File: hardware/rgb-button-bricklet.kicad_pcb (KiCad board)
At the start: 2 copper layers, 25 x 30 mm, 17 parts, among them P1 CON-SENSOR, P2 Boot, SW1 RGB_SWITCH_AD, U1 XMC1XXX24, U2 DRILL, U3 DRILL, U4 DRILL, U5 DRILL

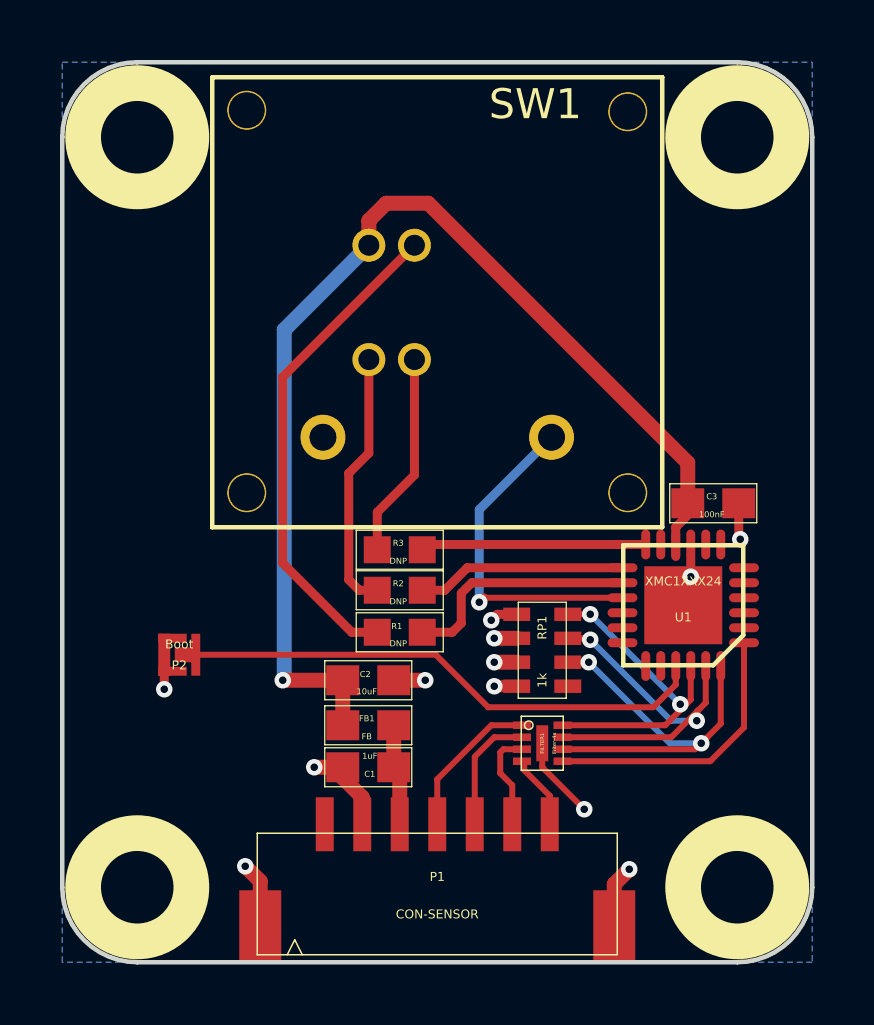
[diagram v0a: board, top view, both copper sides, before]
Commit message: Add fiducial marks and TF logo
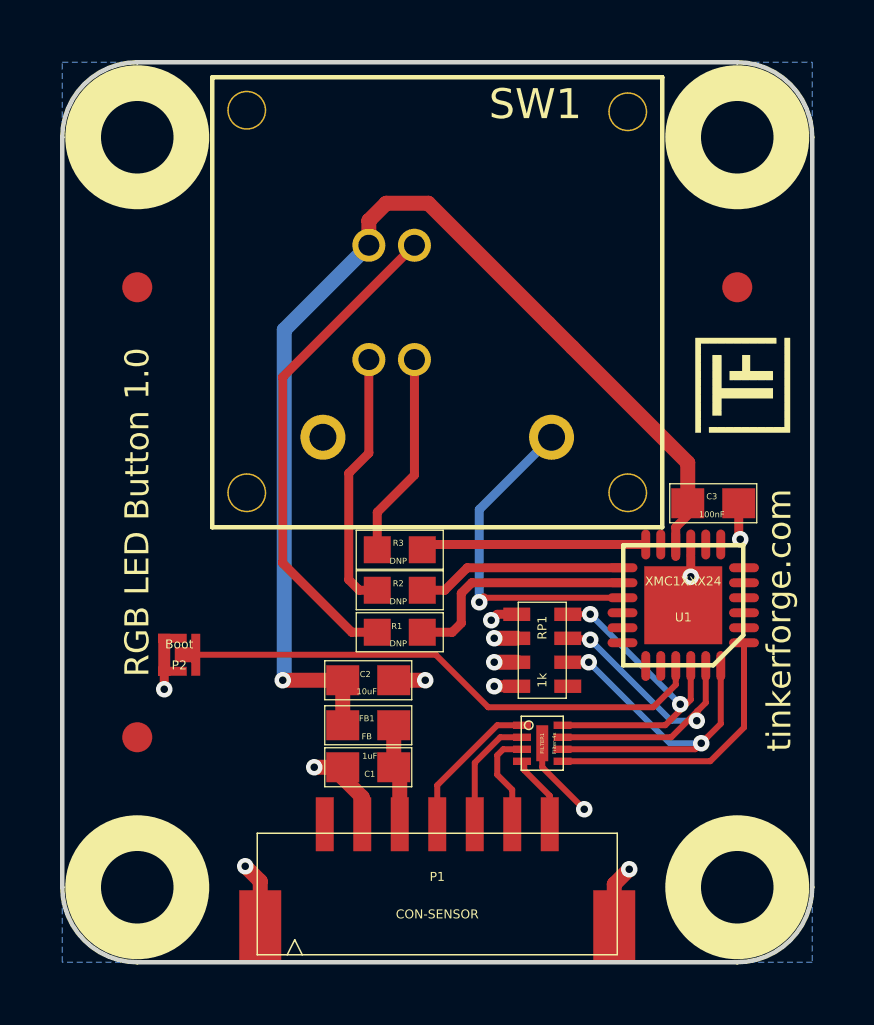
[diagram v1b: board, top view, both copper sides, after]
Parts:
- added Fiducial_Mark: VAL**, kicad-libraries:Fiducial_Mark, F.Cu at (141.7, 92.4)
- added Fiducial_Mark: VAL**, kicad-libraries:Fiducial_Mark, F.Cu at (141.7, 107.4)
- added Fiducial_Mark: VAL**, kicad-libraries:Fiducial_Mark, F.Cu at (161.7, 92.4)
- added G***: Logo_31x31, kicad-libraries:Logo_31x31, F.Cu at (160.3, 97.2)
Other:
- board text added: "RGB LED Button 1.0"
- board text added: "tinkerforge.com"

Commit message: Add WEEE and CE logos
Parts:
- added G***: LOGO, kicad-libraries:WEEE_7mm, B.Cu at (155.4, 92.2)
- added VAL: CE_5mm, kicad-libraries:CE_5mm, B.Cu at (145.9, 92.5)

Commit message: Fix CE logo
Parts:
- turned VAL to 180 degrees
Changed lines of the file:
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@@
   )
   (module kicad-libraries:CE_5mm (layer B.Cu)
-    (at 145.9 92.5)
-    (fp_text reference VAL (at 0 0) (layer B.SilkS) hide
+    (at 145.9 92.5 180)
+    (fp_text reference VAL (at 0 0 180) (layer B.SilkS) hide
       (effects (font (size 1.143 1.143) (thickness 0.1778)) (justify mirror))
     )
-    (fp_text value CE_5mm (at 0 0) (layer B.SilkS) hide
+    (fp_text value CE_5mm (at 0 0 180) (layer B.SilkS) hide
       (effects (font (size 1.143 1.143) (thickness 0.1778)) (justify mirror))
     )

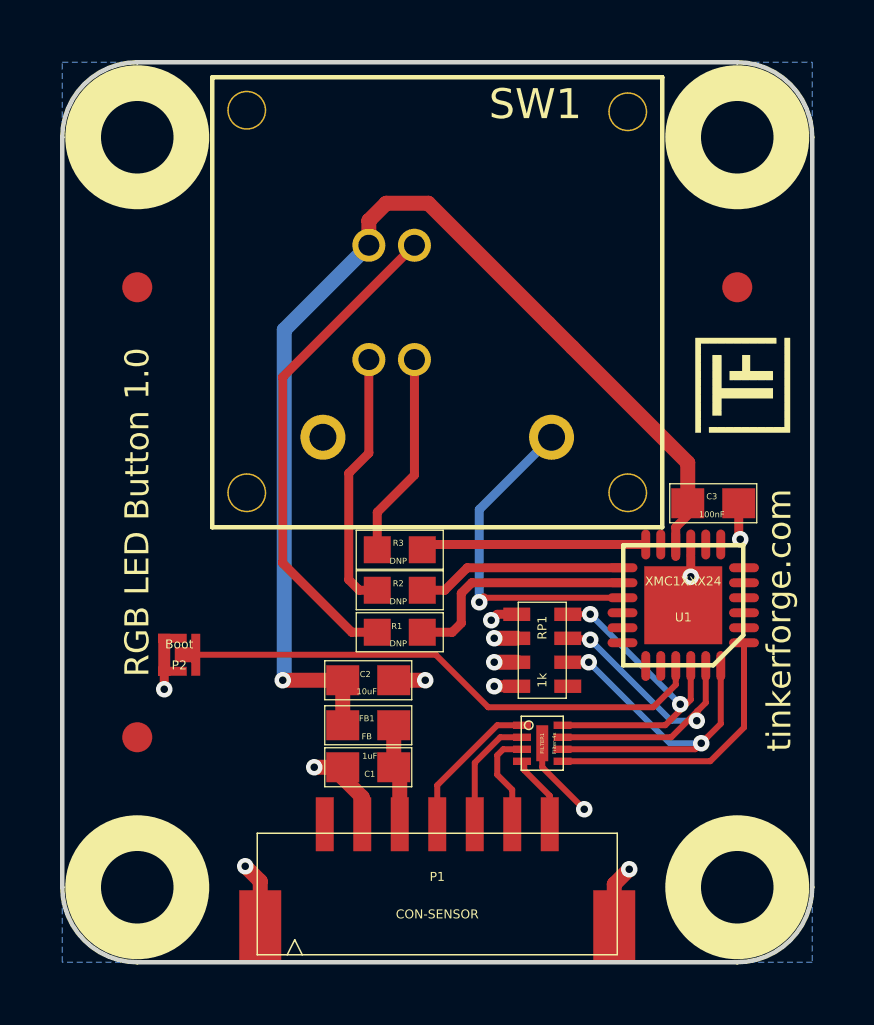
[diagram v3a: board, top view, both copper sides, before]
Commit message: Change filtering to R/C circuit
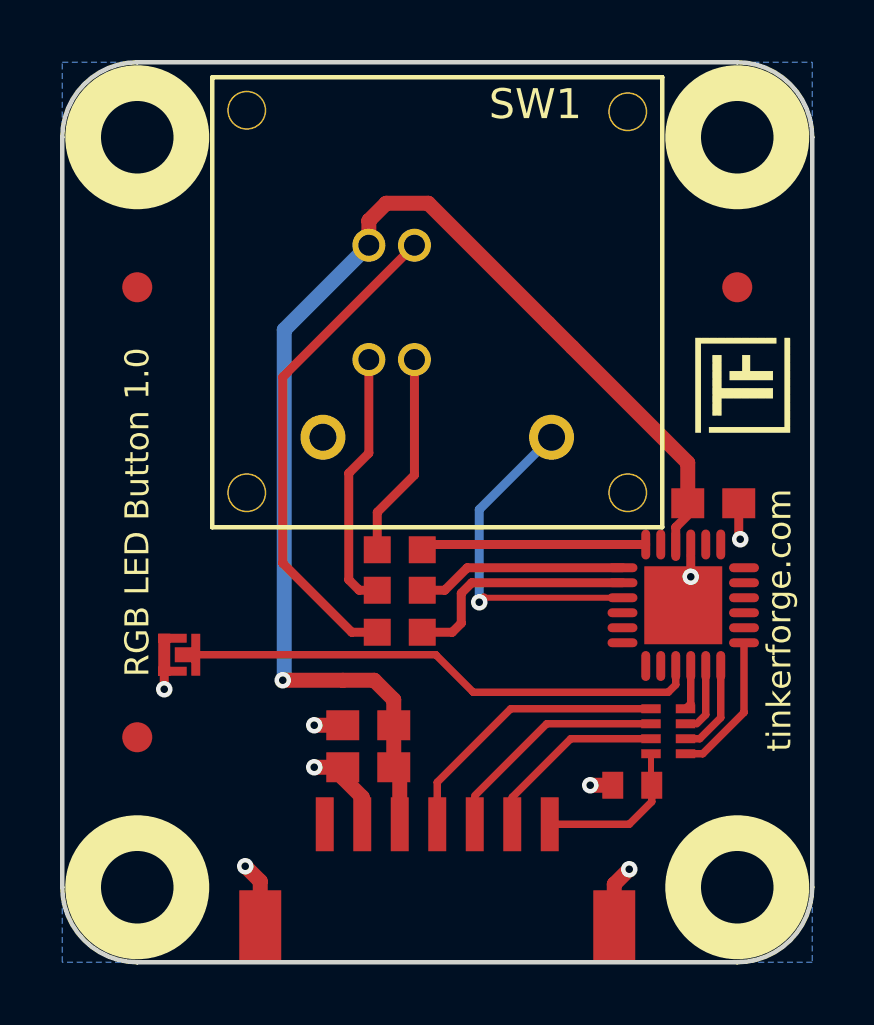
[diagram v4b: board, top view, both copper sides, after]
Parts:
- removed FB1: FB, kicad-libraries:0603E
- removed FILTER1: Filter-4x, kicad-libraries:DFN8-17x135
- added C4: TBD, C0402E, F.Cu at (158.2, 109.0)
- added G***: LOGO, kicad-libraries:Logo_CoMCU, B.Cu at (151.6, 106.9)
- C1, C2, C3: footprint kicad-libraries:0603E -> kicad-libraries:C0603E
- R1, R2, R3: footprint 0603F -> R0603F
- RP1: value 1k -> TBD; footprint 0603X4 -> 4X0402
- moved RP1 4.99 mm to (159.4, 107.2)
- moved C2 1.50 mm to (149.4, 107.0), turned to 0 degrees
- moved G*** 0.25 mm to (155.4, 92.5)
- turned VAL to 0 degrees
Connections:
- C1 pad 2: Net-(C1-Pad2) -> VCC
- P1 pad 3: Net-(C1-Pad2) -> VCC
- P1 pad 4: Net-(FILTER1-Pad1) -> Net-(P1-Pad4)
- P1 pad 5: Net-(FILTER1-Pad2) -> Net-(P1-Pad5)
- P1 pad 6: Net-(FILTER1-Pad3) -> Net-(P1-Pad6)
- P1 pad 7: Net-(FILTER1-Pad4) -> Net-(C4-Pad1)
- RP1 pad 1: Net-(RP1-Pad1) -> Net-(P1-Pad4)
- RP1 pad 2: S-MOSI -> Net-(P1-Pad5)
- RP1 pad 3: S-CLK -> Net-(P1-Pad6)
- RP1 pad 4: S-CS -> Net-(C4-Pad1)
- RP1 pad 5: GND -> S-MISO
- RP1 pad 6: GND -> S-MOSI
- RP1 pad 7: GND -> S-CLK
- RP1 pad 8: GND -> S-CS
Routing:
- net Net-(P1-Pad4): track 0.00 -> 9.54 mm
- net S-MOSI: track 12.7 -> 3.19 mm, vias 2 -> 0
- net S-CLK: track 11.9 -> 2.42 mm, vias 2 -> 0
- net S-CS: track 10.3 -> 1.60 mm, vias 2 -> 0
- net Net-(P1-Pad5): track 0.00 -> 7.72 mm
- net Net-(P1-Pad6): track 0.00 -> 6.83 mm
- net Net-(C4-Pad1): track 0.00 -> 5.97 mm
- net GND: track 18.9 -> 13.6 mm, vias 12 -> 8
- net Net-(FILTER1-Pad1): track 4.95 -> 0.00 mm
- net VCC: track 37.4 -> 42.1 mm
- net S-MISO: track 9.34 -> 4.84 mm
- net Net-(FILTER1-Pad2): track 3.98 -> 0.00 mm
- net Net-(FILTER1-Pad3): track 3.91 -> 0.00 mm
- net Net-(C1-Pad2): track 3.38 -> 0.00 mm
- net Net-(FILTER1-Pad4): track 3.13 -> 0.00 mm

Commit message: Add more 3d information (tbc)
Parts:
- C4: footprint C0402E -> kicad-libraries:C0402E
- R1, R2, R3: footprint R0603F -> kicad-libraries:R0603F
- RP1: footprint 4X0402 -> kicad-libraries:4X0402
- SW1: footprint RGB_SWITCH_AD -> kicad-libraries:RGB_SWITCH_AD

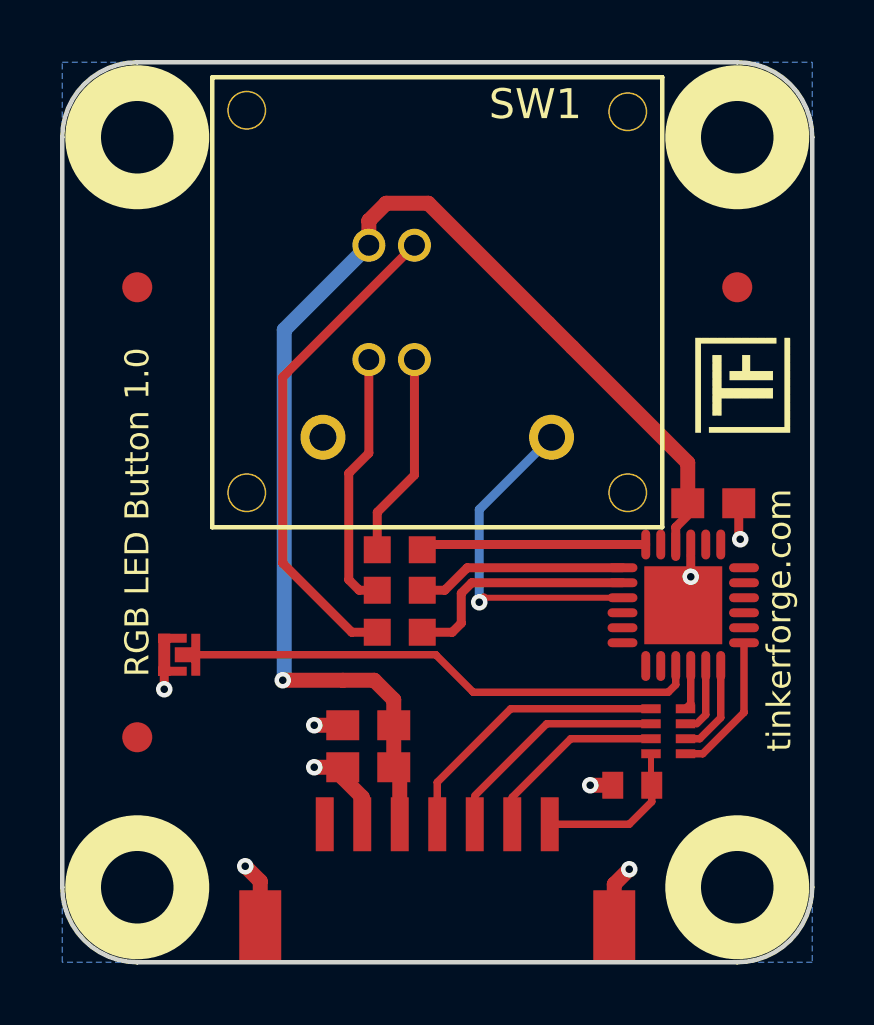
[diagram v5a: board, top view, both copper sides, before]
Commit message: change button footprint, fix design
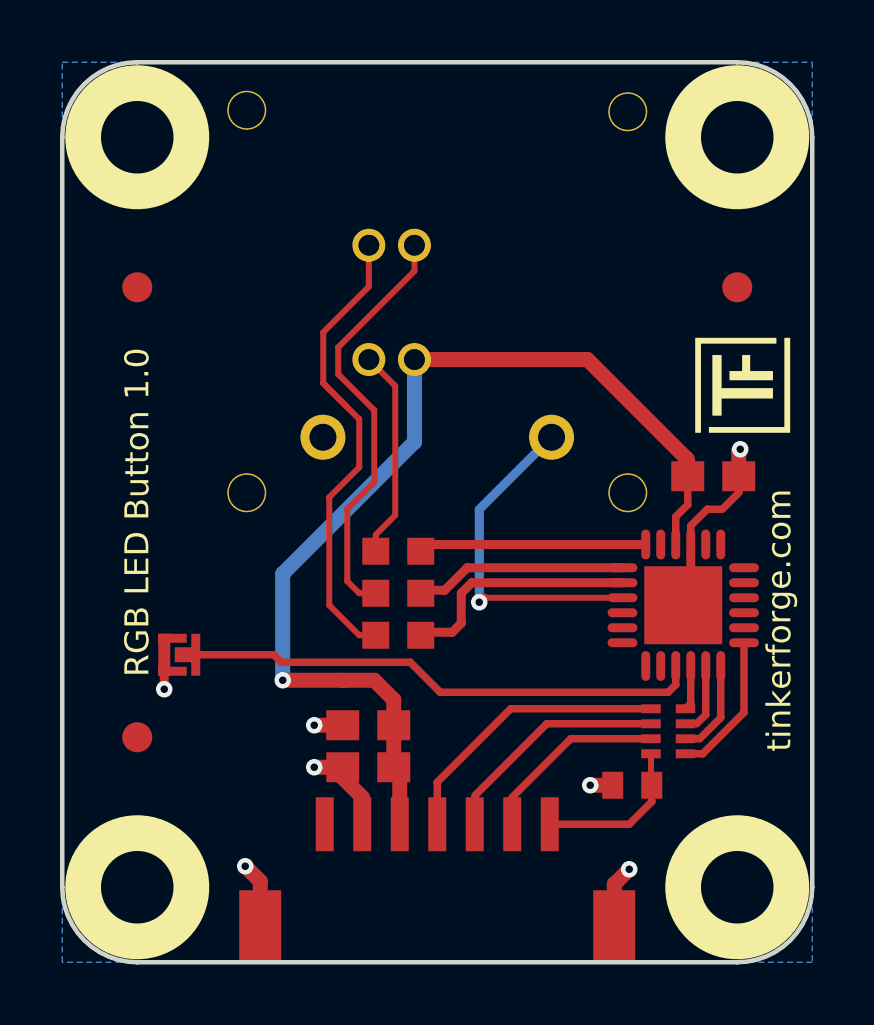
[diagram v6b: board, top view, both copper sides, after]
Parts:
- moved R3 2.85 mm to (150.4, 104.0)
- moved R1 2.70 mm to (150.4, 101.2)
- moved C3 0.90 mm to (160.9, 98.7)
- moved R2 0.11 mm to (150.4, 102.6)
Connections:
- P1 pad 1: Net-(P1-Pad1) -> (no net)
- R1 pad 1: P1.0_HO -> P1.2_HO
- R3 pad 1: P1.2_HO -> P1.0_HO
- U1 pad 11: Net-(U1-Pad11) -> (no net)
- U1 pad 16: Net-(U1-Pad16) -> (no net)
- U1 pad 17: Net-(U1-Pad17) -> (no net)
- U1 pad 18: Net-(U1-Pad18) -> (no net)
- U1 pad 19: Net-(U1-Pad19) -> (no net)
- U1 pad 2: Net-(U1-Pad2) -> (no net)
- U1 pad 20: Net-(U1-Pad20) -> (no net)
- U1 pad 3: Net-(U1-Pad3) -> (no net)
- U1 pad 4: Net-(U1-Pad4) -> (no net)
- U1 pad 5: Net-(U1-Pad5) -> (no net)
- U1 pad 6: Net-(U1-Pad6) -> (no net)
- U1 pad 7: Net-(U1-Pad7) -> (no net)
- U1 pad 8: Net-(U1-Pad8) -> (no net)
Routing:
- net Net-(R3-Pad2): track 7.22 -> 16.6 mm
- net GND: track 13.6 -> 22.6 mm, vias 8 -> 7
- net Net-(R1-Pad2): track 16.5 -> 7.65 mm
- net VCC: track 42.1 -> 34.6 mm
- net Net-(R2-Pad2): track 9.46 -> 14.4 mm

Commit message: add description
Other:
- board text added: "Copyright Tinkerforge GmbH 2017. This documentation describes Open Hardware and is licensed under the CERN OHL v. 1.1. You may redistribute and modify this documentation under the terms of the CERN OHL v.1.1. (http://ohwr.org/cernohl). This documentation is distributed WITHOUT ANY EXPRESS OR IMPLIED WARRANTY, INCLUDING OF MERCHANTABILITY, SATISFACTORY QUALITY AND FITNESS FOR A PARTICULAR PURPOSE.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"
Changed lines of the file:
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@@
     (links 38)
     (no_connects 0)
-    (area 139.124999 84.824999 164.275001 114.975001)
+    (area 138.344999 84.044999 165.055001 115.755001)
     (thickness 1.6)
-    (drawings 10)
+    (drawings 11)
     (tracks 146)
     (zones 0)
@@
   (title_block
     (title "RGB Button Bricklet")
-    (date 2017-05-05)
+    (date 2017-05-08)
     (rev 1.0)
     (company "Tinkerforge GmbH")
@@
       (net 2 VCC))
   )
+  (gr_text "Copyright Tinkerforge GmbH 2017.\nThis documentation describes Open Hardware and is licensed under the\nCERN OHL v. 1.1.\nYou may redistribute and modify this documentation under the terms of the\nCERN OHL v.1.1. (http://ohwr.org/cernohl). This documentation is distributed\nWITHOUT ANY EXPRESS OR IMPLIED WARRANTY, INCLUDING OF\nMERCHANTABILITY, SATISFACTORY QUALITY AND FITNESS FOR A\nPARTICULAR PURPOSE. Please see the CERN OHL v.1.1 for applicable\nconditions" (at 254.9 153.7) (layer Cmts.User)
+    (effects (font (size 0.8 0.8) (thickness 0.15)))
+  )
   (gr_text "RGB LED Button 1.0" (at 141.7 99.9 90) (layer F.SilkS)

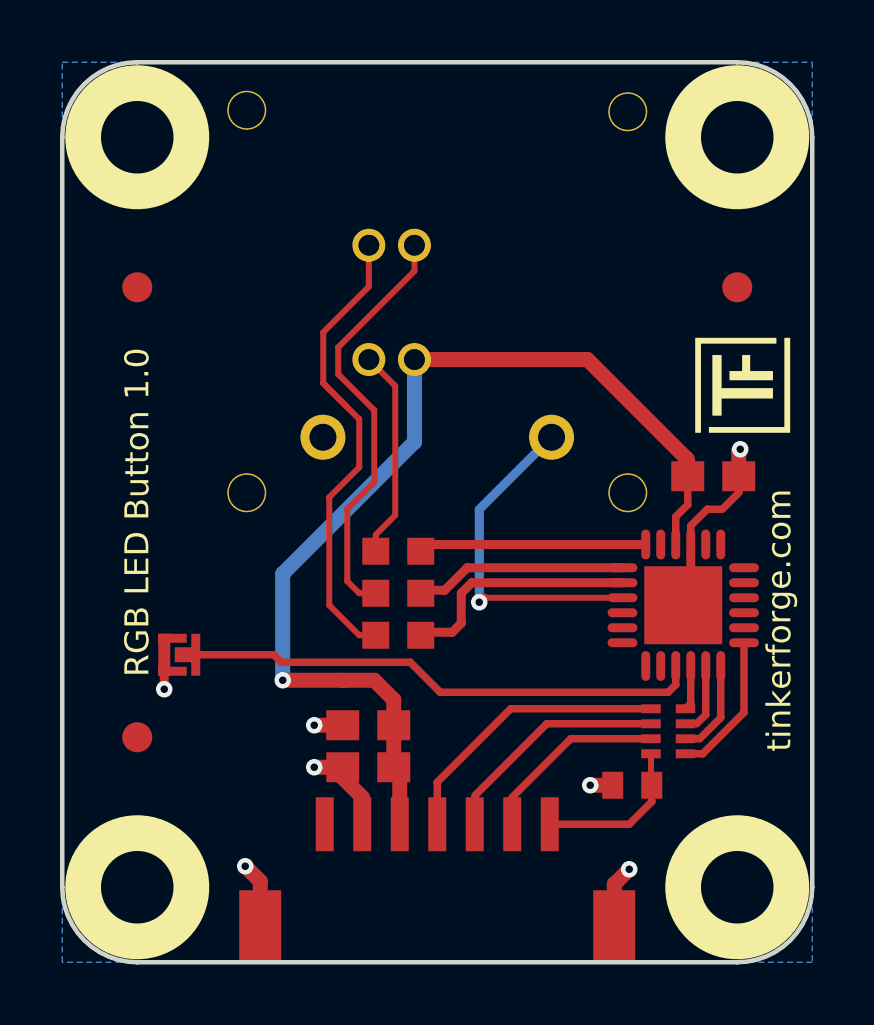
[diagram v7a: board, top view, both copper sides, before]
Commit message: not finished: add led, reduce board size
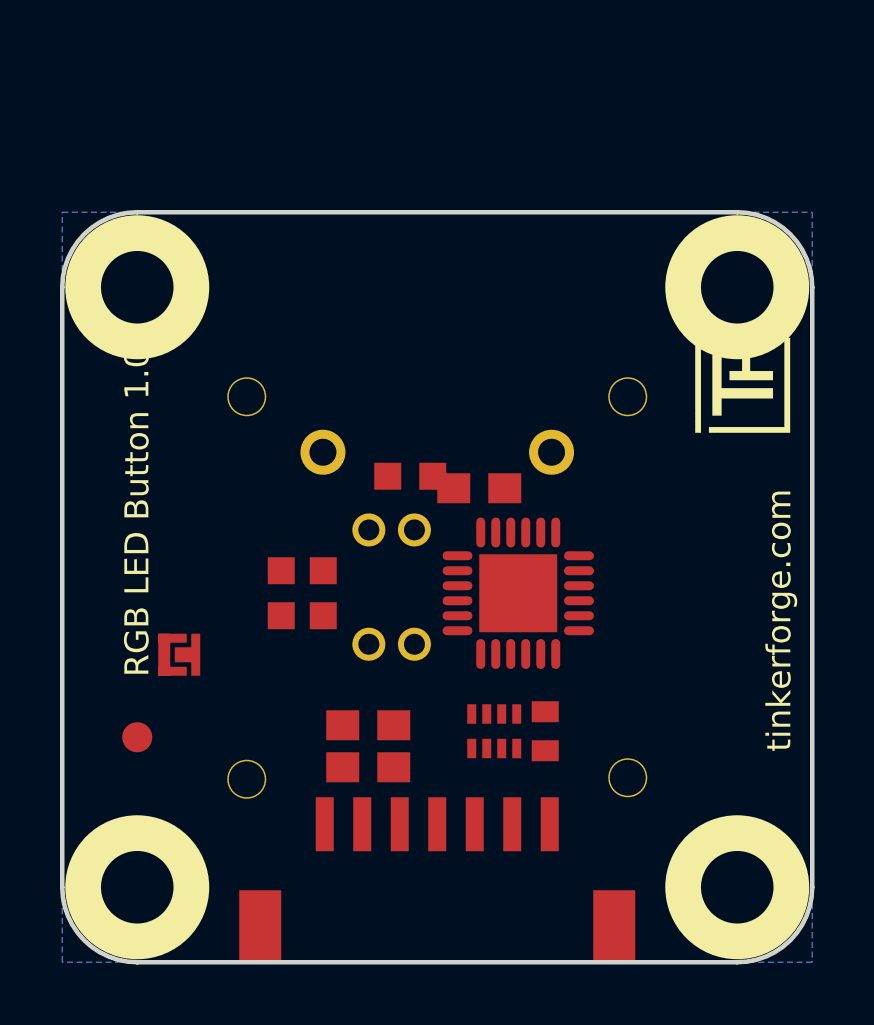
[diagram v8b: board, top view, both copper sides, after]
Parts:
- SW1: moved to B.Cu
- moved SW1 9.50 mm to (151.7, 102.4)
- moved C3 7.81 mm to (153.1, 99.1)
- moved RP1 5.80 mm to (153.6, 107.2), turned to 0 degrees
- moved U1 5.51 mm to (154.4, 102.6)
- moved U2 5.00 mm to (141.7, 92.4)
- moved U3 5.00 mm to (161.7, 92.4)
- moved R2 3.90 mm to (146.5, 102.6), turned to 270 degrees
- moved C4 3.41 mm to (155.3, 107.2), turned to 90 degrees
- moved R3 2.87 mm to (147.9, 102.6), turned to 270 degrees
- moved R1 2.53 mm to (150.8, 98.7)
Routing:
- net VCC: track 34.6 -> 0.00 mm, vias 1 -> 0
- net GND: track 22.6 -> 0.00 mm, vias 7 -> 0
- net Net-(P2-Pad2): track 17.8 -> 0.00 mm
- net Net-(R3-Pad2): track 16.6 -> 0.00 mm
- net Net-(R2-Pad2): track 14.4 -> 0.00 mm
- net PinSwitch: track 11.3 -> 0.00 mm, vias 1 -> 0
- net Net-(P1-Pad4): track 9.54 -> 0.00 mm
- net P1.0_HO: track 7.94 -> 0.00 mm
- net Net-(P1-Pad5): track 7.72 -> 0.00 mm
- net Net-(R1-Pad2): track 7.65 -> 0.00 mm
- net P1.2_HO: track 7.52 -> 0.00 mm
- net P1.1_HO: track 6.99 -> 0.00 mm
- net Net-(P1-Pad6): track 6.83 -> 0.00 mm
- net Net-(C4-Pad1): track 5.97 -> 0.00 mm
- net S-MISO: track 4.84 -> 0.00 mm
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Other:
- board size 25 x 30 mm -> 25 x 25 mm
